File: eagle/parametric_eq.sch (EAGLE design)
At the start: 39 parts, among them IC1 TL072P, IC2 TL072P

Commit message: almost routed
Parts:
- C1, C2, C3, C4, C5, C6, C7, C8, C9: device rcl:C-US025-030X050 -> rcl:C-US050-050X075
- renumbered HI to HIFREQ, LOW to LOWFREQ, MID to MIDFREQ
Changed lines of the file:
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@@
 <part name="IC1" library="linear" deviceset="TL072" device="P"/>
 <part name="IC2" library="linear" deviceset="TL072" device="P"/>
-<part name="C1" library="rcl" deviceset="C-US" device="025-030X050" value="330p"/>
-<part name="C2" library="rcl" deviceset="C-US" device="025-030X050" value="330p"/>
-<part name="C3" library="rcl" deviceset="C-US" device="025-030X050" value="330p"/>
+<part name="C1" library="rcl" deviceset="C-US" device="050-050X075" value="330p"/>
+<part name="C2" library="rcl" deviceset="C-US" device="050-050X075" value="330p"/>
+<part name="C3" library="rcl" deviceset="C-US" device="050-050X075" value="330p"/>
 <part name="R1" library="rcl" deviceset="R-US_" device="0207/10" value="2k2"/>
 <part name="R6" library="rcl" deviceset="R-US_" device="0207/10" value="2k2"/>
 <part name="R7" library="rcl" deviceset="R-US_" device="0207/10" value="2k2"/>
 <part name="R10" library="rcl" deviceset="R-US_" device="0207/10" value="1k"/>
-<part name="C4" library="rcl" deviceset="C-US" device="025-030X050" value="39n"/>
-<part name="C5" library="rcl" deviceset="C-US" device="025-030X050" value="100n"/>
-<part name="C6" library="rcl" deviceset="C-US" device="025-030X050" value="5n6"/>
-<part name="C7" library="rcl" deviceset="C-US" device="025-030X050" value="15n"/>
-<part name="C8" library="rcl" deviceset="C-US" device="025-030X050" value="1n8"/>
-<part name="C9" library="rcl" deviceset="C-US" device="025-030X050" value="4n7"/>
+<part name="C4" library="rcl" deviceset="C-US" device="050-050X075" value="39n"/>
+<part name="C5" library="rcl" deviceset="C-US" device="050-050X075" value="100n"/>
+<part name="C6" library="rcl" deviceset="C-US" device="050-050X075" value="5n6"/>
+<part name="C7" library="rcl" deviceset="C-US" device="050-050X075" value="15n"/>
+<part name="C8" library="rcl" deviceset="C-US" device="050-050X075" value="1n8"/>
+<part name="C9" library="rcl" deviceset="C-US" device="050-050X075" value="4n7"/>
 <part name="R12" library="rcl" deviceset="R-US_" device="0207/10" value="4k7"/>
 <part name="R13" library="rcl" deviceset="R-US_" device="0207/10" value="5k1"/>
@@
 <part name="INPUT" library="erthenvar" deviceset="AUDIO-JACK" device=""/>
 <part name="GND7" library="supply1" deviceset="GND" device=""/>
-<part name="LOW" library="bourns_ptd" deviceset="PTD902" device="" technology="PTD902" value="50k log"/>
-<part name="MID" library="bourns_ptd" deviceset="PTD902" device="" technology="PTD902" value="50k log"/>
-<part name="HI" library="bourns_ptd" deviceset="PTD902" device="" technology="PTD902" value="50k log"/>
+<part name="LOWFREQ" library="bourns_ptd" deviceset="PTD902" device="" technology="PTD902" value="50k log"/>
+<part name="MIDFREQ" library="bourns_ptd" deviceset="PTD902" device="" technology="PTD902" value="50k log"/>
+<part name="HIFREQ" library="bourns_ptd" deviceset="PTD902" device="" technology="PTD902" value="50k log"/>
 <part name="LOLEV" library="bourns_ptd" deviceset="PTD901" device="" value="5k lin"/>
 <part name="MIDLEV" library="bourns_ptd" deviceset="PTD901" device="" value="5k lin"/>
@@
 <instance part="INPUT" gate="G$1" x="-5.08" y="71.12" rot="MR180"/>
 <instance part="GND7" gate="1" x="2.54" y="63.5"/>
-<instance part="LOW" gate="/1" x="58.42" y="30.48" rot="MR180"/>
-<instance part="LOW" gate="/2" x="71.12" y="30.48" rot="MR180"/>
-<instance part="MID" gate="/1" x="101.6" y="30.48" rot="MR180"/>
-<instance part="MID" gate="/2" x="116.84" y="30.48" rot="MR180"/>
-<instance part="HI" gate="/1" x="147.32" y="30.48" rot="MR180"/>
-<instance part="HI" gate="/2" x="160.02" y="30.48" rot="MR180"/>
+<instance part="LOWFREQ" gate="/1" x="58.42" y="30.48" rot="MR180"/>
+<instance part="LOWFREQ" gate="/2" x="71.12" y="30.48" rot="MR180"/>
+<instance part="MIDFREQ" gate="/1" x="101.6" y="30.48" rot="MR180"/>
+<instance part="MIDFREQ" gate="/2" x="116.84" y="30.48" rot="MR180"/>
+<instance part="HIFREQ" gate="/1" x="147.32" y="30.48" rot="MR180"/>
+<instance part="HIFREQ" gate="/2" x="160.02" y="30.48" rot="MR180"/>
 <instance part="LOLEV" gate="G$1" x="71.12" y="-5.08" rot="MR90"/>
 <instance part="MIDLEV" gate="G$1" x="116.84" y="-5.08" rot="MR90"/>
@@
 <pinref part="R13" gate="G$1" pin="2"/>
 <wire x1="58.42" y1="22.86" x2="58.42" y2="25.4" width="0.1524" layer="91"/>
-<pinref part="LOW" gate="/1" pin="E"/>
+<pinref part="LOWFREQ" gate="/1" pin="E"/>
 </segment>
 </net>
@@
 <pinref part="R12" gate="G$1" pin="2"/>
 <wire x1="71.12" y1="22.86" x2="71.12" y2="25.4" width="0.1524" layer="91"/>
-<pinref part="LOW" gate="/2" pin="E"/>
+<pinref part="LOWFREQ" gate="/2" pin="E"/>
 </segment>
 </net>
@@
 <pinref part="R15" gate="G$1" pin="2"/>
 <wire x1="116.84" y1="22.86" x2="116.84" y2="25.4" width="0.1524" layer="91"/>
-<pinref part="MID" gate="/2" pin="E"/>
+<pinref part="MIDFREQ" gate="/2" pin="E"/>
 </segment>
 </net>
@@
 <pinref part="R14" gate="G$1" pin="2"/>
 <wire x1="101.6" y1="22.86" x2="101.6" y2="25.4" width="0.1524" layer="91"/>
-<pinref part="MID" gate="/1" pin="E"/>
+<pinref part="MIDFREQ" gate="/1" pin="E"/>
 </segment>
 </net>
@@
 <pinref part="R19" gate="G$1" pin="2"/>
 <wire x1="147.32" y1="22.86" x2="147.32" y2="25.4" width="0.1524" layer="91"/>
-<pinref part="HI" gate="/1" pin="E"/>
+<pinref part="HIFREQ" gate="/1" pin="E"/>
 </segment>
 </net>
@@
 <pinref part="R20" gate="G$1" pin="2"/>
 <wire x1="160.02" y1="22.86" x2="160.02" y2="25.4" width="0.1524" layer="91"/>
-<pinref part="HI" gate="/2" pin="E"/>
+<pinref part="HIFREQ" gate="/2" pin="E"/>
 </segment>
 </net>
@@
 <wire x1="76.2" y1="38.1" x2="71.12" y2="38.1" width="0.1524" layer="91"/>
 <junction x="71.12" y="38.1"/>
-<pinref part="LOW" gate="/2" pin="A"/>
-<pinref part="LOW" gate="/2" pin="S"/>
-<pinref part="LOW" gate="/1" pin="A"/>
-<pinref part="LOW" gate="/1" pin="S"/>
+<pinref part="LOWFREQ" gate="/2" pin="A"/>
+<pinref part="LOWFREQ" gate="/2" pin="S"/>
+<pinref part="LOWFREQ" gate="/1" pin="A"/>
+<pinref part="LOWFREQ" gate="/1" pin="S"/>
 </segment>
 </net>
@@
 <wire x1="121.92" y1="38.1" x2="116.84" y2="38.1" width="0.1524" layer="91"/>
 <junction x="116.84" y="38.1"/>
-<pinref part="MID" gate="/1" pin="A"/>
-<pinref part="MID" gate="/1" pin="S"/>
-<pinref part="MID" gate="/2" pin="A"/>
-<pinref part="MID" gate="/2" pin="S"/>
+<pinref part="MIDFREQ" gate="/1" pin="A"/>
+<pinref part="MIDFREQ" gate="/1" pin="S"/>
+<pinref part="MIDFREQ" gate="/2" pin="A"/>
+<pinref part="MIDFREQ" gate="/2" pin="S"/>
 </segment>
 </net>
@@
 <wire x1="165.1" y1="38.1" x2="160.02" y2="38.1" width="0.1524" layer="91"/>
 <junction x="160.02" y="38.1"/>
-<pinref part="HI" gate="/1" pin="A"/>
-<pinref part="HI" gate="/1" pin="S"/>
-<pinref part="HI" gate="/2" pin="A"/>
-<pinref part="HI" gate="/2" pin="S"/>
-</segment>
-</net>
+<pinref part="HIFREQ" gate="/1" pin="A"/>
+<pinref part="HIFREQ" gate="/1" pin="S"/>
+<pinref part="HIFREQ" gate="/2" pin="A"/>
+<pinref part="HIFREQ" gate="/2" pin="S"/>
+</segment>
+</net>

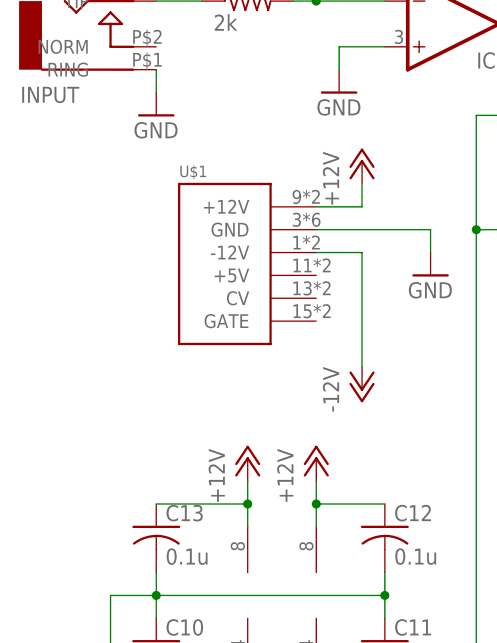
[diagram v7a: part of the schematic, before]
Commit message: power filter caps
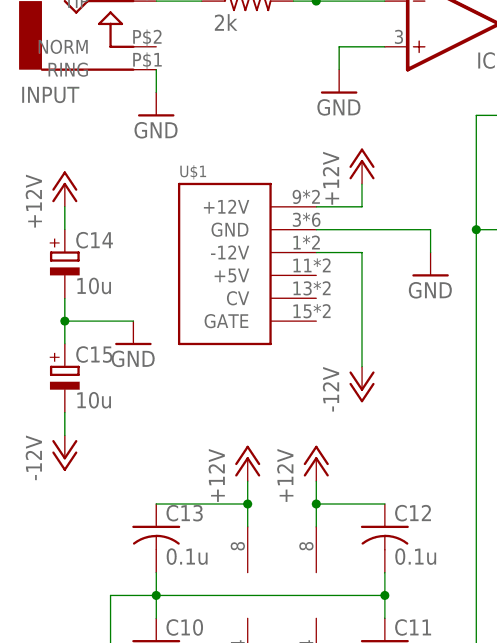
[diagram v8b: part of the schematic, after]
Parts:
- added C14, C15: 10u, rcl:CPOL-EUB45181A
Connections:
- net +12V: now also C14.+
- net -12V: now also C15.-
- net GND: now also C14.-, C15.+
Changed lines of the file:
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@@
 <part name="HILEV" library="bourns_ptd" deviceset="PTD901" device="" value="5k lin"/>
 <part name="GAIN" library="bourns_ptd" deviceset="PTD901" device="" value="5k lin"/>
+<part name="P+4" library="supply1" deviceset="+12V" device=""/>
+<part name="P-4" library="supply1" deviceset="-12V" device=""/>
+<part name="C14" library="rcl" deviceset="CPOL-EU" device="B45181A" value="10u"/>
+<part name="C15" library="rcl" deviceset="CPOL-EU" device="B45181A" value="10u"/>
+<part name="GND8" library="supply1" deviceset="GND" device=""/>
 </parts>
 <sheets>
@@
 <instance part="HILEV" gate="G$1" x="160.02" y="-5.08" rot="MR90"/>
 <instance part="GAIN" gate="G$1" x="40.64" y="91.44" rot="R270"/>
+<instance part="P+4" gate="1" x="-7.62" y="55.88"/>
+<instance part="P-4" gate="1" x="-7.62" y="25.4"/>
+<instance part="C14" gate="G$1" x="-7.62" y="48.26"/>
+<instance part="C15" gate="G$1" x="-7.62" y="35.56"/>
+<instance part="GND8" gate="1" x="0" y="38.1"/>
 </instances>
 <busses>
@@
 <wire x1="25.4" y1="53.34" x2="25.4" y2="55.88" width="0.1524" layer="91"/>
 </segment>
+<segment>
+<pinref part="P+4" gate="1" pin="+12V"/>
+<pinref part="C14" gate="G$1" pin="+"/>
+<wire x1="-7.62" y1="50.8" x2="-7.62" y2="53.34" width="0.1524" layer="91"/>
+</segment>
 </net>
 <net name="-12V" class="0">
@@
 <wire x1="20.32" y1="48.26" x2="25.4" y2="48.26" width="0.1524" layer="91"/>
 <wire x1="25.4" y1="48.26" x2="25.4" y2="35.56" width="0.1524" layer="91"/>
+</segment>
+<segment>
+<pinref part="P-4" gate="1" pin="-12V"/>
+<pinref part="C15" gate="G$1" pin="-"/>
+<wire x1="-7.62" y1="30.48" x2="-7.62" y2="27.94" width="0.1524" layer="91"/>
 </segment>
 </net>
@@
 <wire x1="2.54" y1="66.04" x2="2.54" y2="68.58" width="0.1524" layer="91"/>
 </segment>
-</net>
+<segment>
+<pinref part="C15" gate="G$1" pin="+"/>
+<pinref part="C14" gate="G$1" pin="-"/>
+<wire x1="-7.62" y1="43.18" x2="-7.62" y2="40.64" width="0.1524" layer="91"/>
+<pinref part="GND8" gate="1" pin="GND"/>
+<wire x1="-7.62" y1="40.64" x2="-7.62" y2="38.1" width="0.1524" layer="91"/>
+<wire x1="0" y1="40.64" x2="-7.62" y2="40.64" width="0.1524" layer="91"/>
+<junction x="-7.62" y="40.64"/>
+</segment>
+</net>
